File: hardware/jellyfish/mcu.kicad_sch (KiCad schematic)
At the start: 38 parts, among them SW1 BOOTSEL, U3 RP2040, U4 W25Q128JVS, Y1 12MHz

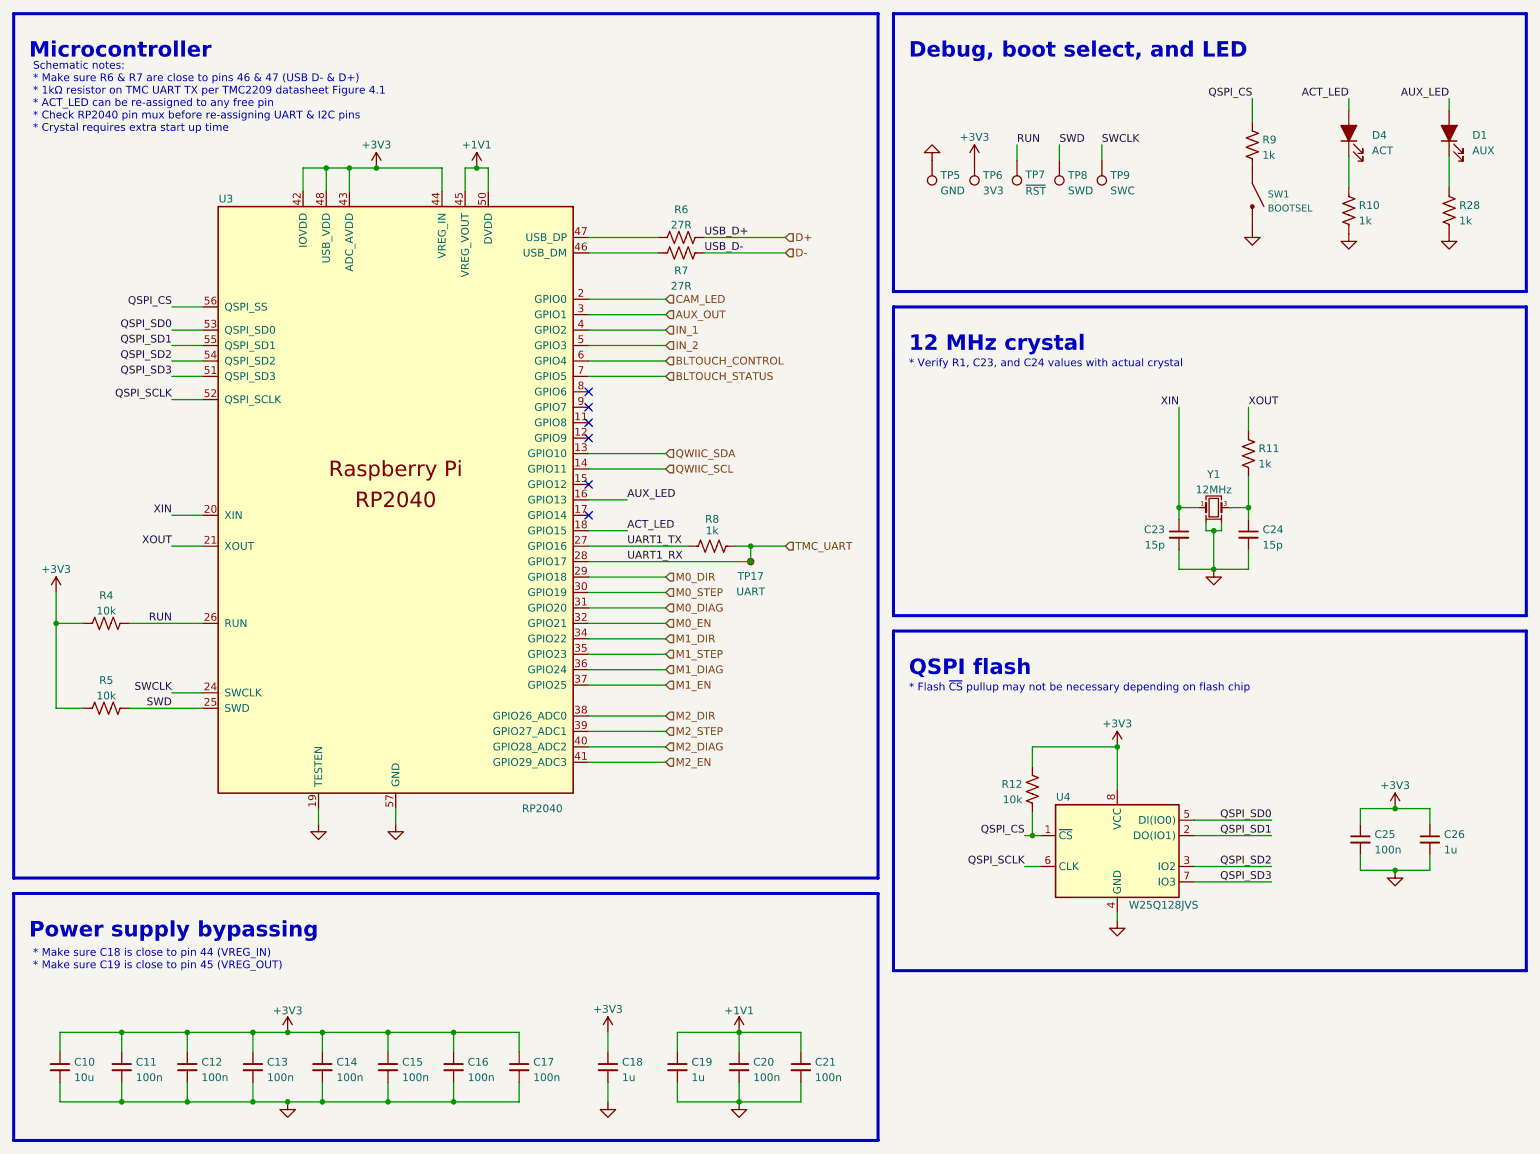
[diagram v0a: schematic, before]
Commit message: Update Jellyfish with some stuff from Starfish
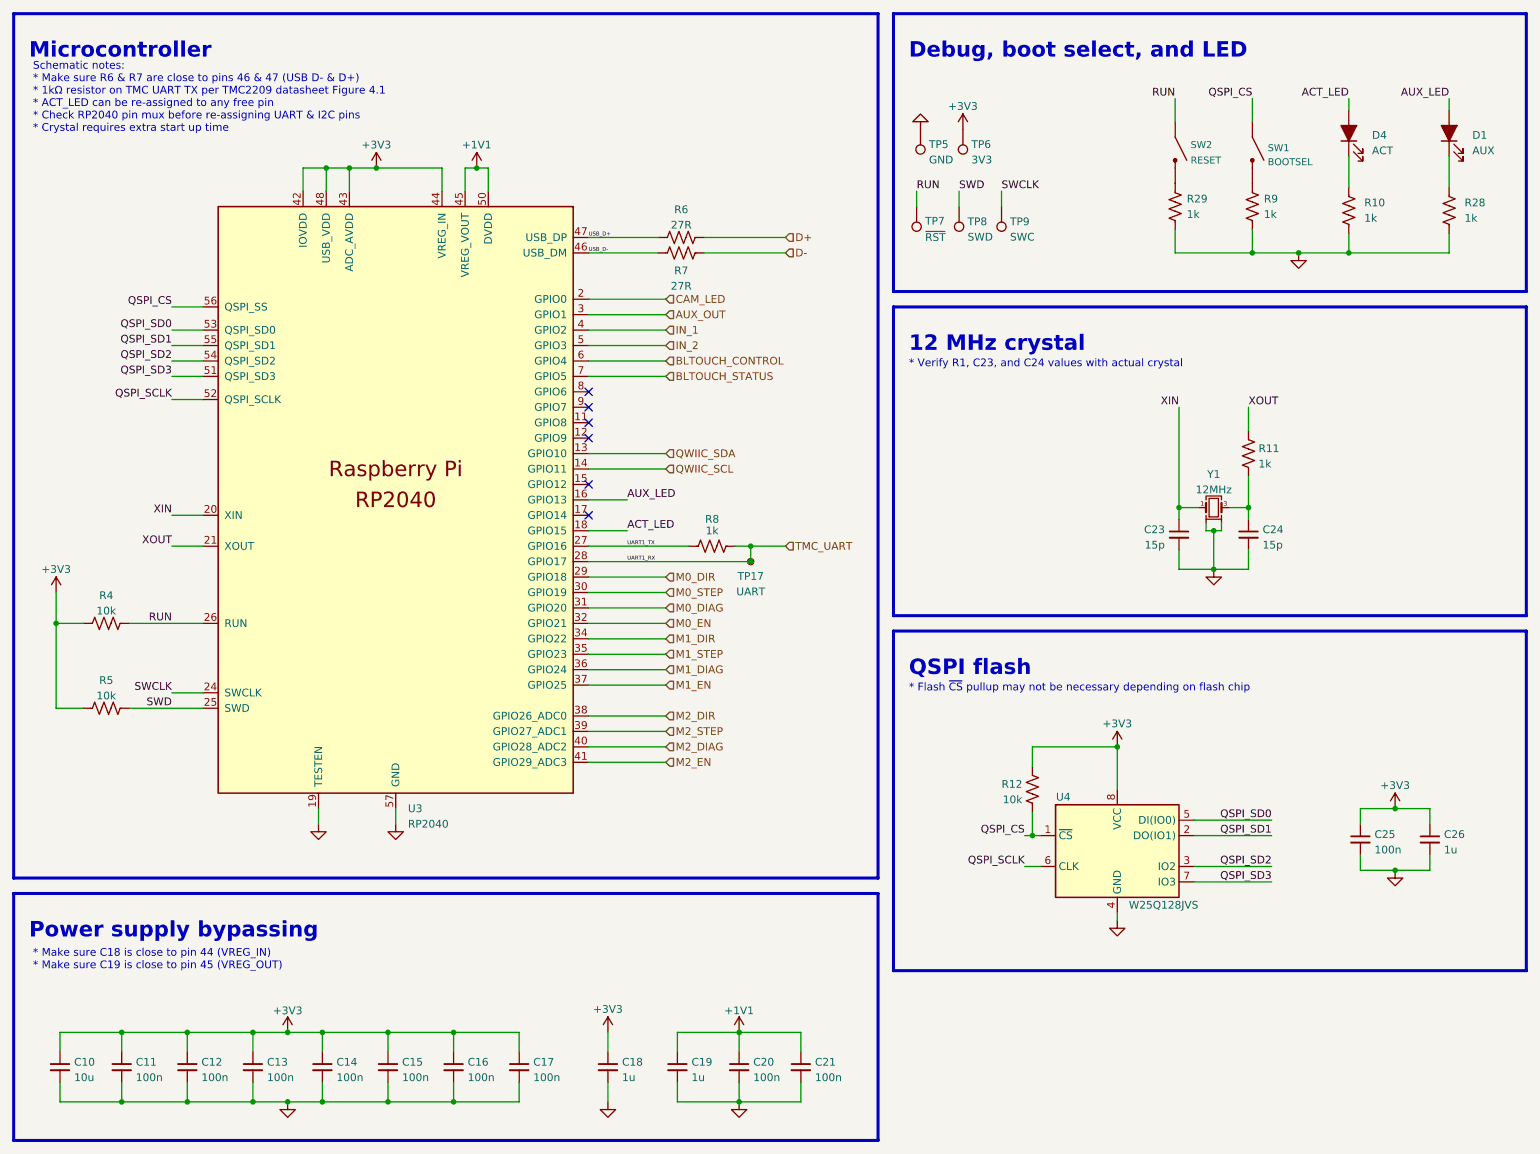
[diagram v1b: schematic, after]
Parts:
- added R29: 1k, winterbloom:R_0402_HandSolder, symbol Device:R_US
- added SW2: RESET, winterbloom:Tactile_Switch_4.2mm, symbol winterbloom:Tactile_Switch
- C10: footprint Capacitor_SMD:C_0805_2012Metric_Pad1.18x1.45mm_HandSolder -> winterbloom:C_0805_HandSolder
- C11, C12, C13, C14, C15, C16, C17, C18, C19, C20, C21, C23, C24, C25, C26: footprint Capacitor_SMD:C_0402_1005Metric_Pad0.74x0.62mm_HandSolder -> winterbloom:C_0402_HandSolder
- R10, R28: footprint Resistor_SMD:R_0603_1608Metric_Pad0.98x0.95mm_HandSolder -> winterbloom:R_0603_HandSolder
- R11, R12, R4, R5, R6, R7, R8, R9: footprint Resistor_SMD:R_0402_1005Metric_Pad0.72x0.64mm_HandSolder -> winterbloom:R_0402_HandSolder
- SW1: MPN (none) -> MF-SW-TACT-4.2MM, MF-SW-TACT-6MM
- U3: symbol MCU_RaspberryPi_RP2040:RP2040 -> winterbloom:RP2040
- Y1: MPN (none) -> ABM8G-106-12.000MHZ-T
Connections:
- net GND: now also R9.1, R29.1; no longer SW1.2
- net QSPI_CS: now also SW1.1; no longer R9.2
- net RUN: now also SW2.1
- net USB_D-: now reaches R7.2, U3.46 (USB_DM)
- net USB_D+: now reaches R6.2, U3.47 (USB_DP)
- new net: R29.2, SW2.2
- new net: R9.2, SW1.2
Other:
- moved on the sheet: R9, SW1, TP5, TP6, TP7, TP8, TP9
